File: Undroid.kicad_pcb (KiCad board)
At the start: 2 copper layers, 64.1 x 143.1 mm, 47 parts, among them J1 AudioJack2, J2 JAE_SIM_Card_SF72S006, U2 AS4C256M16D3

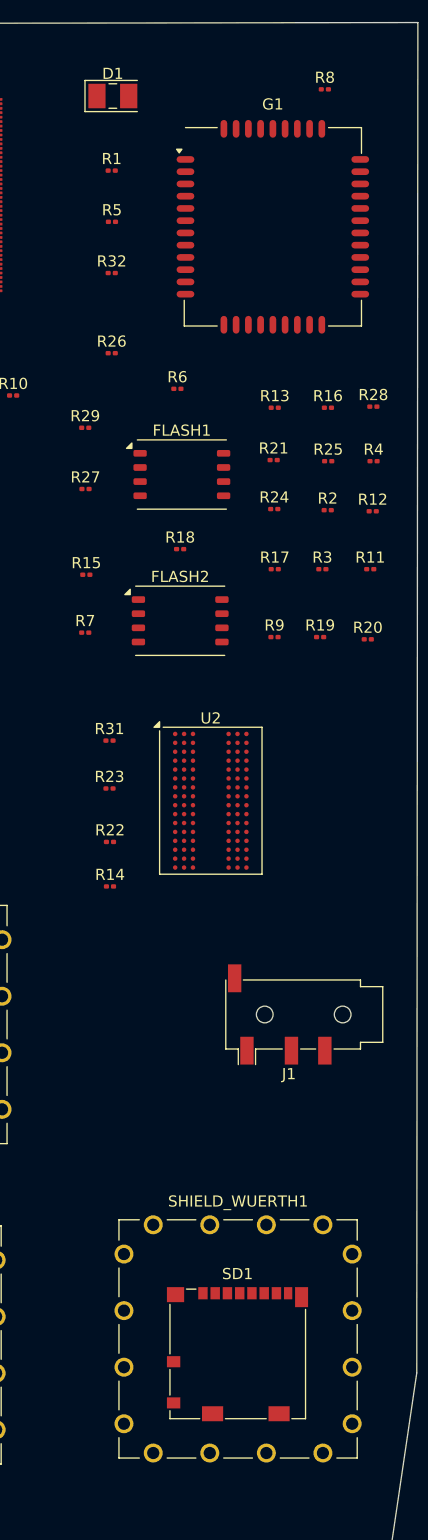
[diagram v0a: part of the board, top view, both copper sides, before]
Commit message: ZET-0001: Working on it, need to route now, and test it.
Signed-off-by: Amlal EL Mahrouss <amlal@softwarelabs.com>
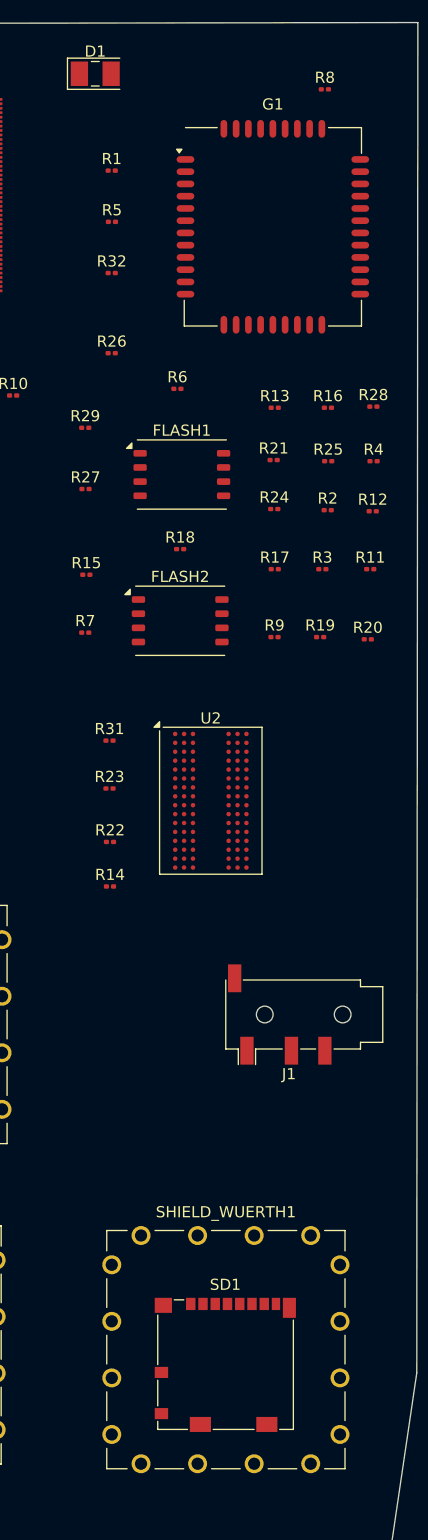
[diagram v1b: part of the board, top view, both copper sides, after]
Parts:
- moved D1 2.55 mm to (151.1, 43.2)
- moved SD1 1.46 mm to (162.8, 159.2)
- moved SHIELD_WUERTH1 1.46 mm to (162.9, 157.8)
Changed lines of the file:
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@@
 	(footprint "LED_SMD:LED_PLCC-2_3x2mm_AK"
 		(layer "F.Cu")
-		(at 152.7 45.2)
+		(at 151.125 43.2)
 		(descr "LED, SMD, PLCC-2, 3.0 x 2.0mm, orientation marker at anode, https://media.digikey.com/pdf/Data%20Sheets/CREE%20Power/CLM3A-BKW,GKW.pdf")
 		(tags "LED PLCC-2 SMD")
@@
 	(footprint "Connector_Card:microSD_HC_Molex_104031-0811"
 		(layer "F.Cu")
-		(at 163.9 158.1875)
+		(at 162.805 159.15)
 		(descr "1.10mm Pitch microSD Memory Card Connector, Surface Mount, Push-Pull Type, 1.42mm Height, with Detect Switch (https://www.molex.com/pdm_docs/sd/1040310811_sd.pdf)")
 		(tags "microSD SD molex")
@@
 	(footprint "RF_Shielding:Wuerth_36503205_20x20mm"
 		(layer "F.Cu")
-		(at 163.95 156.84)
+		(at 162.855 157.8025)
 		(descr "WE-SHC Shielding Cabinet THT 21x21mm")
 		(tags "Shielding Cabinet")

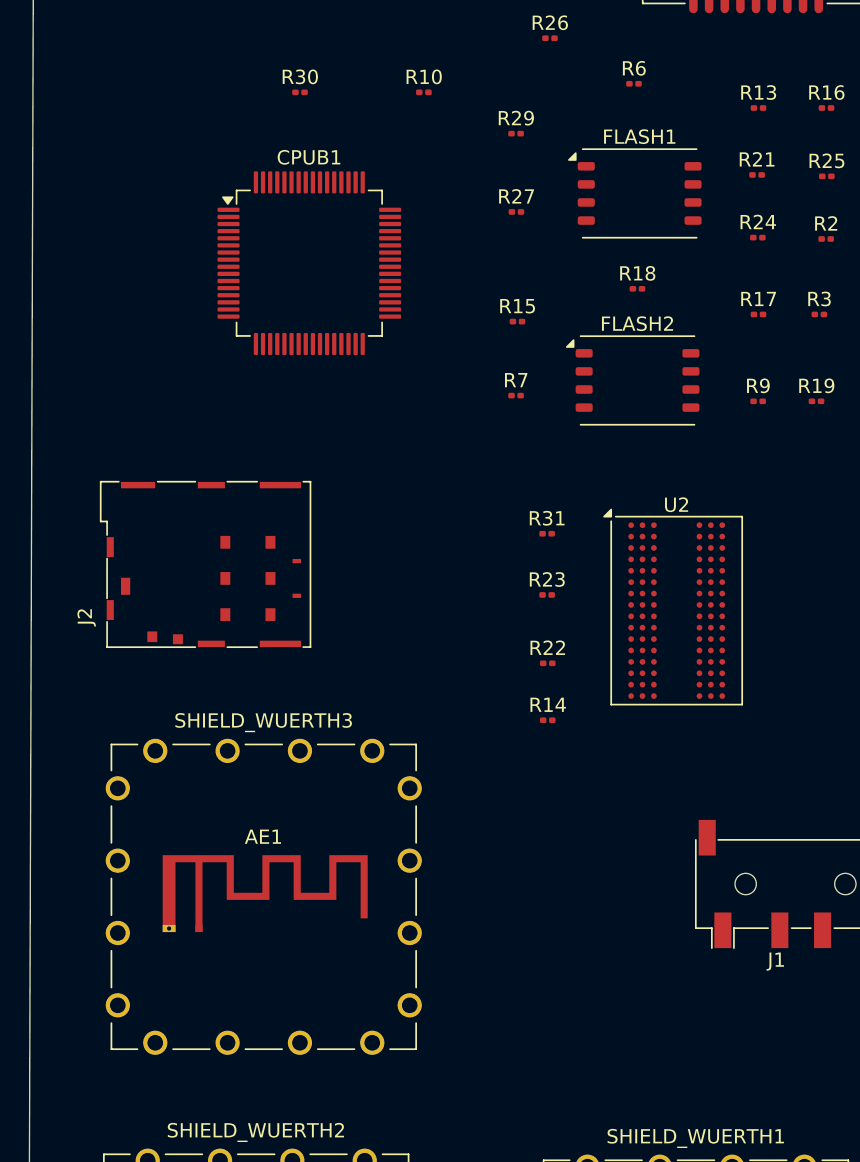
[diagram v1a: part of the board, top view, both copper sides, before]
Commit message: main: Doing DRC and ERC right now...
Signed-off-by: Amlal EL Mahrouss <amlal@softwarelabs.com>
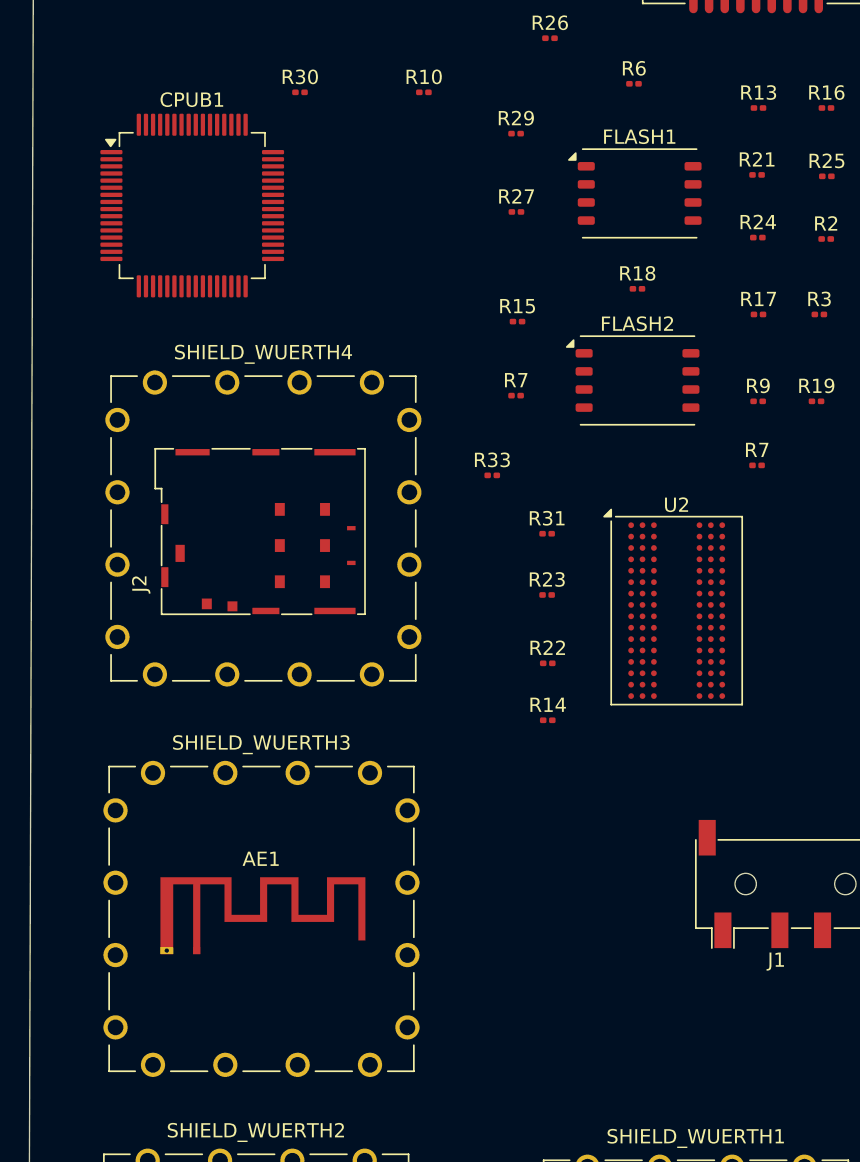
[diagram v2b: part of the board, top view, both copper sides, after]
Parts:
- added R33: R, Resistor_SMD:R_0201_0603Metric, F.Cu at (148.5, 99.0)
- added R7: R, Resistor_SMD:R_0201_0603Metric, F.Cu at (167.1, 98.3)
- added SHIELD_WUERTH4: RFShield_OnePiece, RF_Shielding:Wuerth_36503205_20x20mm, F.Cu at (132.5, 102.7)
- moved CPUB1 9.17 mm to (127.5, 80.0)
- moved J2 4.47 mm to (134.3, 103.9)
- moved AE1 1.56 mm to (127.8, 132.4)
- moved SHIELD_WUERTH3 1.56 mm to (132.3, 130.2)
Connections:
- net RAM_CA_REF renamed VREFCA
- net RAM_DQ_REF renamed VREFDQ
- CPU2 pad 158: NMI -> unconnected-(CPU2A-NMI_N-Pad158)
- CPU2 pad 159: PWR_RESET_BUT -> RESET
- CPU2 pad 28: GND -> unconnected-(CPU2A-DDR3_DM1-Pad28)
- CPU2 pad 29: GND -> unconnected-(CPU2A-DDR3_DM0-Pad29)
- CPU2 pad 31: GND -> RAM_UDQS
- CPU2 pad 32: GND -> RAM_UDQS_N
- CPU2 pad 33: GND -> RAM_LDQS
- CPU2 pad 34: GND -> RAM_LDQS_N
- CPU2 pad 74: Net-(CPU2A-HPOUTL) -> unconnected-(CPU2A-HPOUTL-Pad74)
- CPU2 pad 75: Net-(CPU2A-HPBP) -> unconnected-(CPU2A-HPBP-Pad75)
- CPU2 pad 76: Net-(CPU2A-V33_HP) -> Net-(CPU2A-SVREF)
- CPU2 pad 77: Net-(CPU2A-HPCOM) -> unconnected-(CPU2A-HPCOM-Pad77)
- CPU2 pad 78: Net-(CPU2A-HPOUTR) -> unconnected-(CPU2A-HPOUTR-Pad78)
- CPU2 pad 79: Net-(CPU2A-AGND) -> unconnected-(CPU2A-AGND-Pad79)
- CPU2 pad 80: GND -> unconnected-(CPU2A-VRP-Pad80)
- CPU2 pad 82: GND -> unconnected-(CPU2A-VRA2-Pad82)
- CPU2 pad 83: GND -> unconnected-(CPU2A-VRA1-Pad83)
- CPU2 pad 85: Net-(CPU2A-VMIC) -> Net-(CPU2A-SVREF)
- CPU2 pad 93: GND -> unconnected-(CPU2A-UDM0-Pad93)
- CPU2 pad 94: GND -> unconnected-(CPU2A-UDP0-Pad94)
- CPU2 pad 95: GND -> unconnected-(CPU2A-UDM1-Pad95)
- CPU2 pad 96: GND -> unconnected-(CPU2A-UDP1-Pad96)
- CPU2 pad 97: Net-(CPU2A-V33_USB) -> Net-(CPU2A-SVREF)
- CPUB1 pad 36: PWR_RESET -> RESET
- CPUB1 pad 59: GND -> unconnected-(CPUB1-DM-Pad59)
- CPUB1 pad 60: GND -> unconnected-(CPUB1-DP-Pad60)
- G1 pad 11: GND -> unconnected-(G1-RTC_GPIO0-Pad11)
- G1 pad 18: GSM_GEN -> unconnected-(G1-SIM_VDD-Pad18)
- G1 pad 25: GND -> unconnected-(G1-USB_DP-Pad25)
- G1 pad 26: GND -> unconnected-(G1-USB_DM-Pad26)
- G1 pad 28: GSM_RST_MOD -> unconnected-(G1-~{RESET}-Pad28)
- G1 pad 39: GSM_PWR_MOD -> GND
- G1 pad 40: Net-(G1-VDD_EXT) -> unconnected-(G1-VDD_EXT-Pad40)
- J2 pad C1: +3.3V -> Net-(J2-VCC)
- J2 pad CSW: GSM_CSW -> unconnected-(J2-PadCSW)
- J2 pad DSW: GSM_DSW -> unconnected-(J2-PadDSW)
- J2 pad SH: unconnected-(J2-PadSH) -> Net-(SHIELD_WUERTH4-Shield)
- POWERC1 pad A9: +3.3V -> VBUS_USBC
- POWERC1 pad B9: +3.3V -> VBUS_USBC
- R11 pad 1: Net-(FLASH2-VDD) -> VBUS_USBC
- R11 pad 2: +3.3V -> Net-(FLASH2-VDD)
- R12 pad 1: +3.3V -> VBUS_USBC
- R13 pad 2: +3.3V -> VBUS_USBC
- R19 pad 1: VDDQ -> VBUS_USBC
- R32 pad 2: Net-(CPU2A-VMIC) -> Net-(CPU2A-SVREF)
- R4 pad 2: +3.3V -> VBUS_USBC
- R6 pad 1: Net-(G1-VDD_3V3) -> +3.3V
- R6 pad 2: +3.3V -> Net-(G1-VDD_3V3)
- R8 pad 1: Net-(G1-VBAT-Pad34) -> +3.3V
- R8 pad 2: +3.3V -> Net-(G1-VBAT-Pad34)
- U2 pad B2: Net-(R17-Pad2) -> Net-(R7-Pad1)
- U2 pad D9: Net-(R17-Pad2) -> Net-(R7-Pad1)
- U2 pad G7: Net-(R17-Pad2) -> Net-(R7-Pad1)
- U2 pad K2: Net-(R17-Pad2) -> Net-(R7-Pad1)
- U2 pad K8: Net-(R17-Pad2) -> Net-(R7-Pad1)
- U2 pad N1: Net-(R17-Pad2) -> Net-(R7-Pad1)
- U2 pad N9: Net-(R17-Pad2) -> Net-(R7-Pad1)
- U2 pad R1: Net-(R17-Pad2) -> Net-(R7-Pad1)
- U2 pad R9: Net-(R17-Pad2) -> Net-(R7-Pad1)

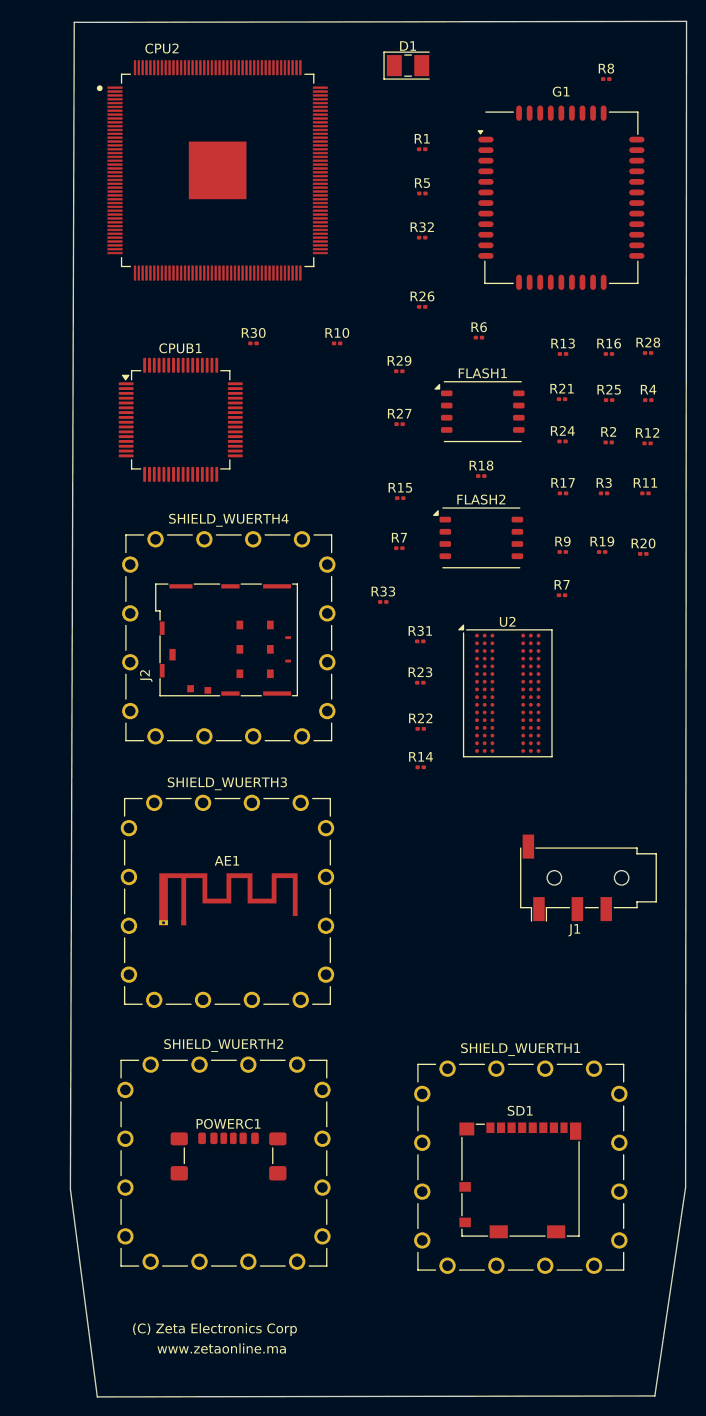
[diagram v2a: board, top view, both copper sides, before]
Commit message: Adding Resistive touch screen and making it sure that it will pass ERC.
Signed-off-by: Amlal EL Mahrouss <amlalelmahrouss@icloud.com>
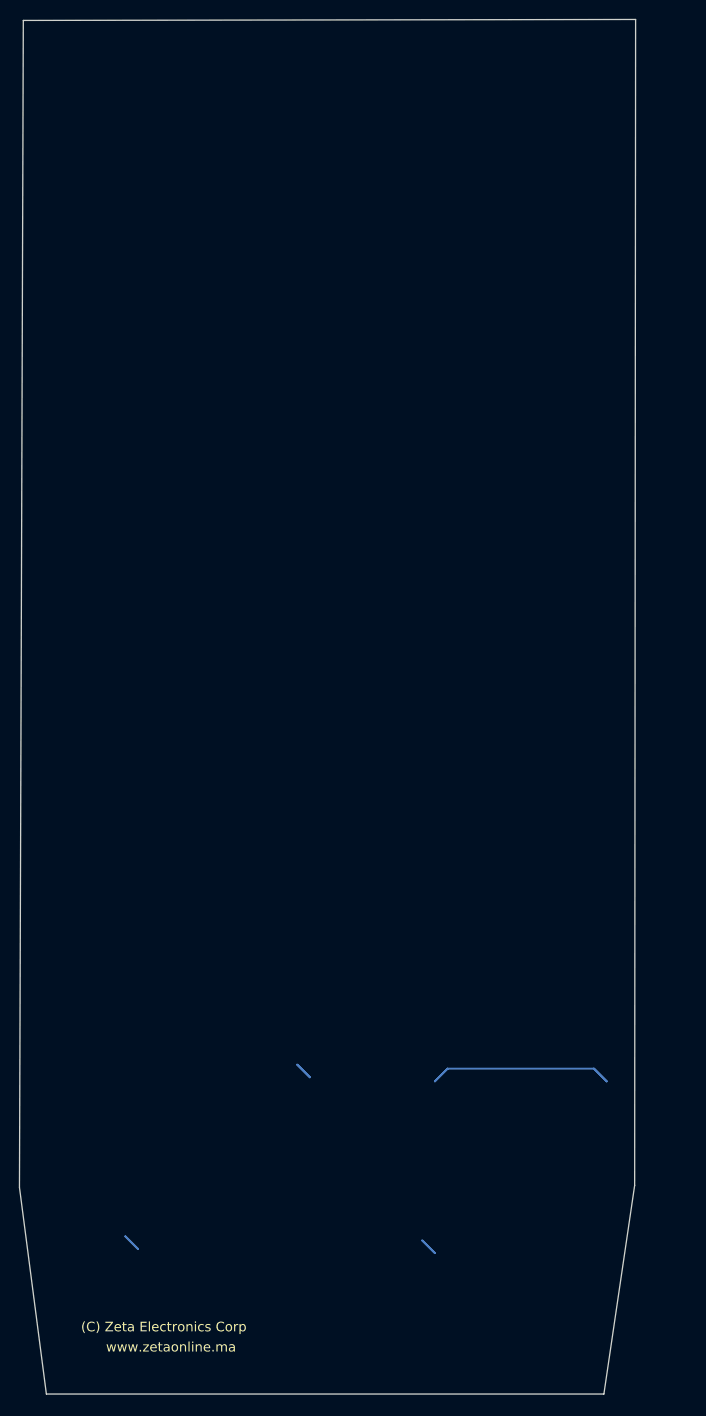
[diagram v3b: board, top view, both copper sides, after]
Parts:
- removed AE1: Antenna_Shield, RF_Antenna:Texas_SWRA117D_2.4GHz_Right
- removed CPU2: Allwinner-A13, Allwinner:QFP40P2200X2200X160-177N
- removed CPUB1: ATSAME70J19A-AN, Package_QFP:LQFP-64_10x10mm_P0.5mm
- removed D1: LED, LED_SMD:LED_PLCC-2_3x2mm_AK
- removed FLASH1, FLASH2: XTSD08G, Package_LGA:LGA-8_8x6mm_P1.27mm
- removed G1: SIM7020C, RF_GSM:SIMCom_SIM800C
- removed J1: AudioJack2, Connector_Audio:Jack_3.5mm_PJ320D_Horizontal
- removed J2: JAE_SIM_Card_SF72S006, Connector_JAE:JAE_SIM_Card_SF72S006
- removed POWERC1: USB_C_Receptacle_PowerOnly_6P, Connector_USB:USB_C_Receptacle_GCT_USB4135-GF-A_6P_TopMnt_Horizontal
- removed R1, R10, R11, R12, R13, R14, R15, R16, R17, R18, R19, R2, R20, R21, R22, R23, R24, R25, R26, R27, R28, R29, R3, R30, R31, R32, R33, R4, R5, R6, R7 (x2), R8, R9: R, Resistor_SMD:R_0201_0603Metric
- removed SD1: Micro_SD_Card, Connector_Card:microSD_HC_Molex_104031-0811
- removed SHIELD_WUERTH1, SHIELD_WUERTH2, SHIELD_WUERTH3, SHIELD_WUERTH4: RFShield_OnePiece, RF_Shielding:Wuerth_36503205_20x20mm
- removed U2: AS4C256M16D3, Package_BGA:BGA-96_9.0x13.0mm_Layout2x3x16_P0.8mm
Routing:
- net Net-(SD1-SHIELD): track 0.00 -> 26.4 mm
- net Net-(POWERC1-SHIELD): track 0.00 -> 7.44 mm
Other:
- board size 64.1 x 143.1 mm -> 64.1 x 143 mm
- copper layers 2 -> 4
